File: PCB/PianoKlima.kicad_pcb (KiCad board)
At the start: 2 copper layers, 1 part, among them U1 ESP32-WROVER

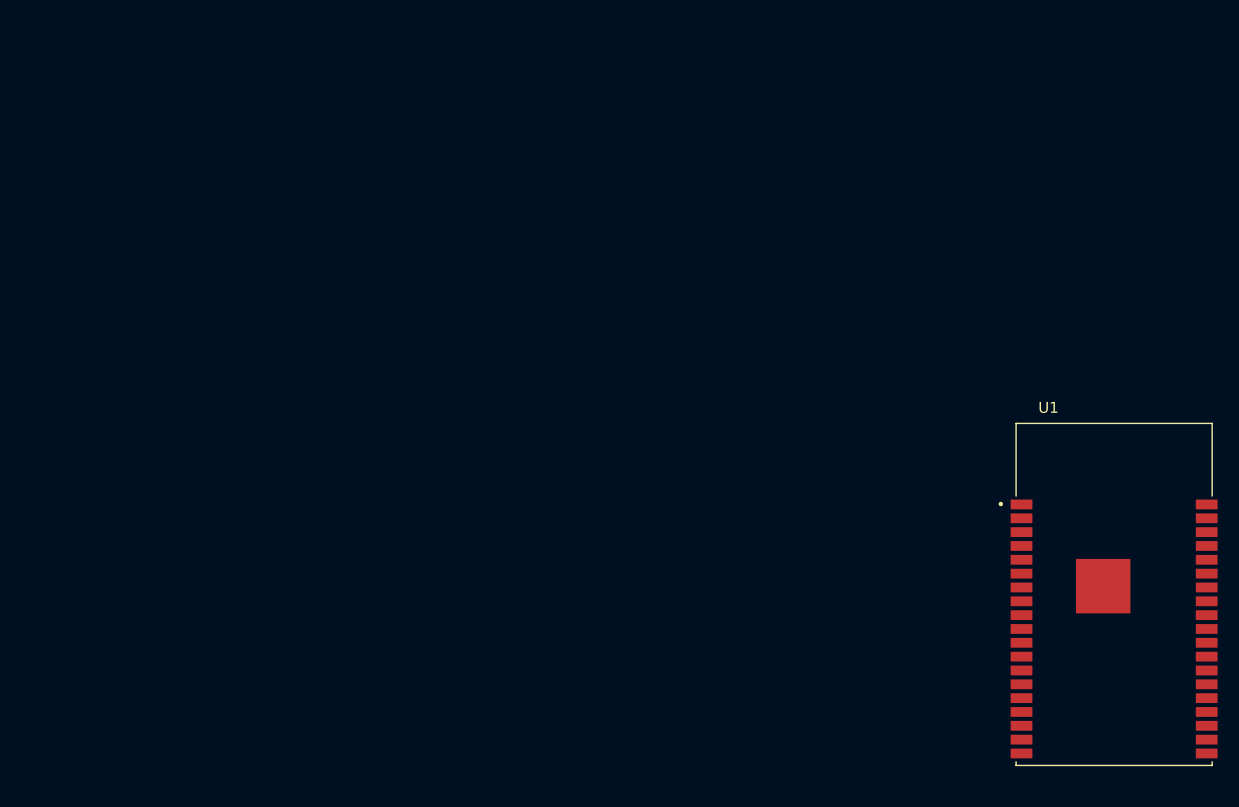
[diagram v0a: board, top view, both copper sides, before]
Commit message: Use the latest Kicad version
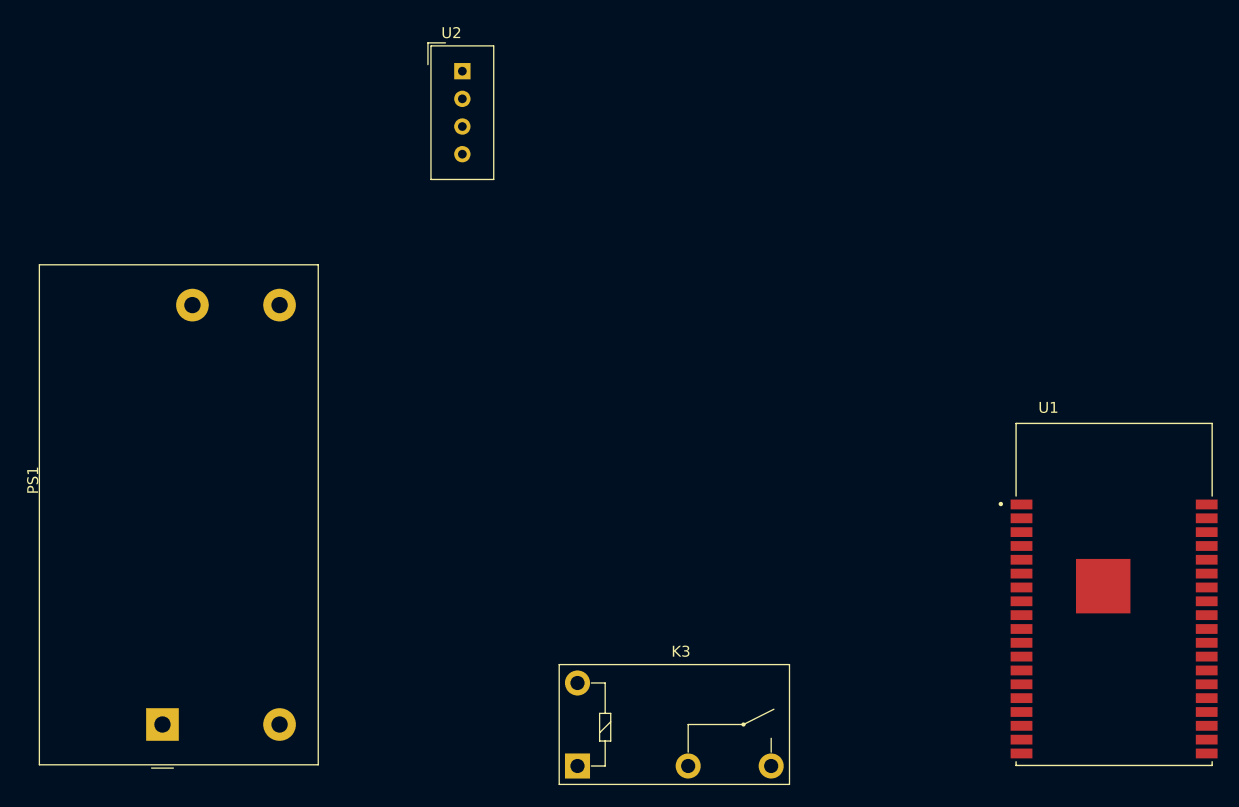
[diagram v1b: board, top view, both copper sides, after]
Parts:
- added K3: G5Q-1A, Relay_THT:Relay_SPST_Omron-G5Q-1A, F.Cu at (97.8, 95.2)
- added PS1: IRM-05-5, Converter_ACDC:Converter_ACDC_MeanWell_IRM-05-xx_THT, F.Cu at (59.7, 91.4)
- added U2: DHT11, Sensor:Aosong_DHT11_5.5x12.0_P2.54mm, F.Cu at (87.2, 31.5)
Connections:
- U1 pad 1: Net-(U1-Pad1) -> unconnected-(U1-Pad1)
- U1 pad 10: Net-(U1-Pad10) -> unconnected-(U1-Pad10)
- U1 pad 11: Net-(U1-Pad11) -> unconnected-(U1-Pad11)
- U1 pad 12: Net-(U1-Pad12) -> unconnected-(U1-Pad12)
- U1 pad 13: Net-(U1-Pad13) -> unconnected-(U1-Pad13)
- U1 pad 14: Net-(U1-Pad14) -> unconnected-(U1-Pad14)
- U1 pad 15: Net-(U1-Pad15) -> unconnected-(U1-Pad15)
- U1 pad 16: Net-(U1-Pad16) -> unconnected-(U1-Pad16)
- U1 pad 17: Net-(U1-Pad17) -> unconnected-(U1-Pad17)
- U1 pad 18: Net-(U1-Pad18) -> unconnected-(U1-Pad18)
- U1 pad 19: Net-(U1-Pad19) -> unconnected-(U1-Pad19)
- U1 pad 2: Net-(U1-Pad2) -> unconnected-(U1-Pad2)
- U1 pad 20: Net-(U1-Pad20) -> unconnected-(U1-Pad20)
- U1 pad 21: Net-(U1-Pad21) -> unconnected-(U1-Pad21)
- U1 pad 22: Net-(U1-Pad22) -> unconnected-(U1-Pad22)
- U1 pad 23: Net-(U1-Pad23) -> unconnected-(U1-Pad23)
- U1 pad 24: Net-(U1-Pad24) -> unconnected-(U1-Pad24)
- U1 pad 25: Net-(U1-Pad25) -> unconnected-(U1-Pad25)
- U1 pad 26: Net-(U1-Pad26) -> unconnected-(U1-Pad26)
- U1 pad 27: Net-(U1-Pad27) -> unconnected-(U1-Pad27)
- U1 pad 28: Net-(U1-Pad28) -> unconnected-(U1-Pad28)
- U1 pad 29: Net-(U1-Pad29) -> unconnected-(U1-Pad29)
- U1 pad 3: Net-(U1-Pad3) -> unconnected-(U1-Pad3)
- U1 pad 30: Net-(U1-Pad30) -> unconnected-(U1-Pad30)
- U1 pad 31: Net-(U1-Pad31) -> unconnected-(U1-Pad31)
- U1 pad 32: Net-(U1-Pad32) -> unconnected-(U1-Pad32)
- U1 pad 33: Net-(U1-Pad33) -> unconnected-(U1-Pad33)
- U1 pad 34: Net-(U1-Pad34) -> unconnected-(U1-Pad34)
- U1 pad 35: Net-(U1-Pad35) -> unconnected-(U1-Pad35)
- U1 pad 36: Net-(U1-Pad36) -> unconnected-(U1-Pad36)
- U1 pad 37: Net-(U1-Pad37) -> unconnected-(U1-Pad37)
- U1 pad 38: Net-(U1-Pad38) -> unconnected-(U1-Pad38)
- U1 pad 39: Net-(U1-Pad39) -> unconnected-(U1-Pad39)
- U1 pad 4: Net-(U1-Pad4) -> unconnected-(U1-Pad4)
- U1 pad 5: Net-(U1-Pad5) -> unconnected-(U1-Pad5)
- U1 pad 6: Net-(U1-Pad6) -> unconnected-(U1-Pad6)
- U1 pad 7: Net-(U1-Pad7) -> unconnected-(U1-Pad7)
- U1 pad 8: Net-(U1-Pad8) -> unconnected-(U1-Pad8)
- U1 pad 9: Net-(U1-Pad9) -> unconnected-(U1-Pad9)
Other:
- net class Default removed
